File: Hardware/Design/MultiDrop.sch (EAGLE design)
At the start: 26 parts

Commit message: Hardware: ^9 rdy for review
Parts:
- removed SD1: SD, Documentation:SD
- added D3: DAYNIGHT, D-LED:LED5MM
- added D4: STATUS, D-LED:LED5MM
- added K1, K2, K3: (no value), L-PWR:L0805
- added U$12: FT, Documentation:FT
- D1: value (none) -> DAYNIGHT; device D-SBR:DSMC -> D-LED:LED5MM
- D2: value (none) -> STATUS; device D-SBR:DSMC -> D-LED:LED5MM
- R1, R2, R3, R4: value 50 -> 49.9
- U$11: value TT -> PT; device Documentation:TT -> Documentation:PT
- U$4: value FT -> K3; device Documentation:FT -> Documentation:K3
- U$6: value PT -> TT; device Documentation:PT -> Documentation:TT
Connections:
- removed net N$27: BM1.SPI, SD1.PV_PWR
- new net BL: K1.1, U$4.K1
- new net BL-WHT: K1.2, U$4.COM
- new net GN: K3.1, U$4.K3
- new net GN-WHT: K3.2
- new net N$40: BM1.0V@5, D2.K
- new net N$42: BM1.PWR, U$9.+BAT
- new net N$46: BM1.0V@6, D1.K
- new net N$47: BM1.17MA@0, U$5.PWR
- new net N$49: BM1.ICP1, U$5.PL
- new net N$50: BM1.20MA@0, U$6.PWR
- new net N$51: BM1.ADC0, R1.1, U$6.4TO20
- new net N$52: BM1.ADC1, R2.1, U$11.PWR
- new net N$53: BM1.20MA@1, U$11.4TO20
- new net N$54: BM3.20MA@2, BM3.ADC2, D4.A
- new net N$55: BM3.20MA@3, BM3.ADC3, D3.A
- new net N$56: BM3.0V@5, D4.K
- new net N$57: BM3.0V@6, D3.K
- new net OG: K2.1, U$4.K2
- new net OG-WHT: K2.2
- net N$12: now also BM1.0V@2, PV2.-PV, U$9.-BAT; no longer BM3.PWR, D2.K, U$7.BAT_PWR
- net N$13: now also BM3.0V@2, PV4.-PV, U$7.-BAT; no longer D2.A, PV4.PV_PWR
- net N$15: now also BM3.ALT, PV4.+PV; no longer BM1.PWR, D1.K, U$9.BAT_PWR
- net N$16: now also BM3.PWR, U$7.+BAT; no longer D1.A, PV2.PV_PWR
- net N$17: now also BM1.5V, U$4.SUPPLY, U$4.VCC; no longer BM1.0V@3, R1.2, R2.1
- net N$19: now also BM1.DIO13, U$4.E3; no longer BM1.20MA@0, U$11.PWR
- net N$20: now also BM1.0V@3, R1.2, R2.2, U$4.!E1, U$4.!E2, U$4.0V, U$4.0V@1; no longer BM1.ADC0, R1.1, U$11.4TO20
- net N$22: now also BM1.ALT, PV2.+PV; no longer BM1.0V@4, U$4.0V
- net N$23: now also BM3.17MA@0, U$12.PWR; no longer BM1.ICP1, U$4.OC
- net N$24: now also BM1.DIO10, U$4.A0; no longer BM1.17MA@0, U$4.PWR
- net N$25: now also BM1.DIO11, U$4.A1; no longer BM1.ADC1, R2.2, U$6.PWR
- net N$26: now also BM1.DIO12, U$4.A2; no longer BM1.20MA@1, U$6.4TO20
- net N$35: now also BM3.ICP1, U$12.PL; no longer BM3.0V@4, U$5.0V
- net N$36: now also BM1.20MA@2, BM1.ADC2, D2.A; no longer BM3.ICP1, U$5.OC
- net N$37: now also BM1.20MA@3, BM1.ADC3, D1.A; no longer BM3.17MA@0, U$5.PWR
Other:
- moved on the sheet: R1, R2

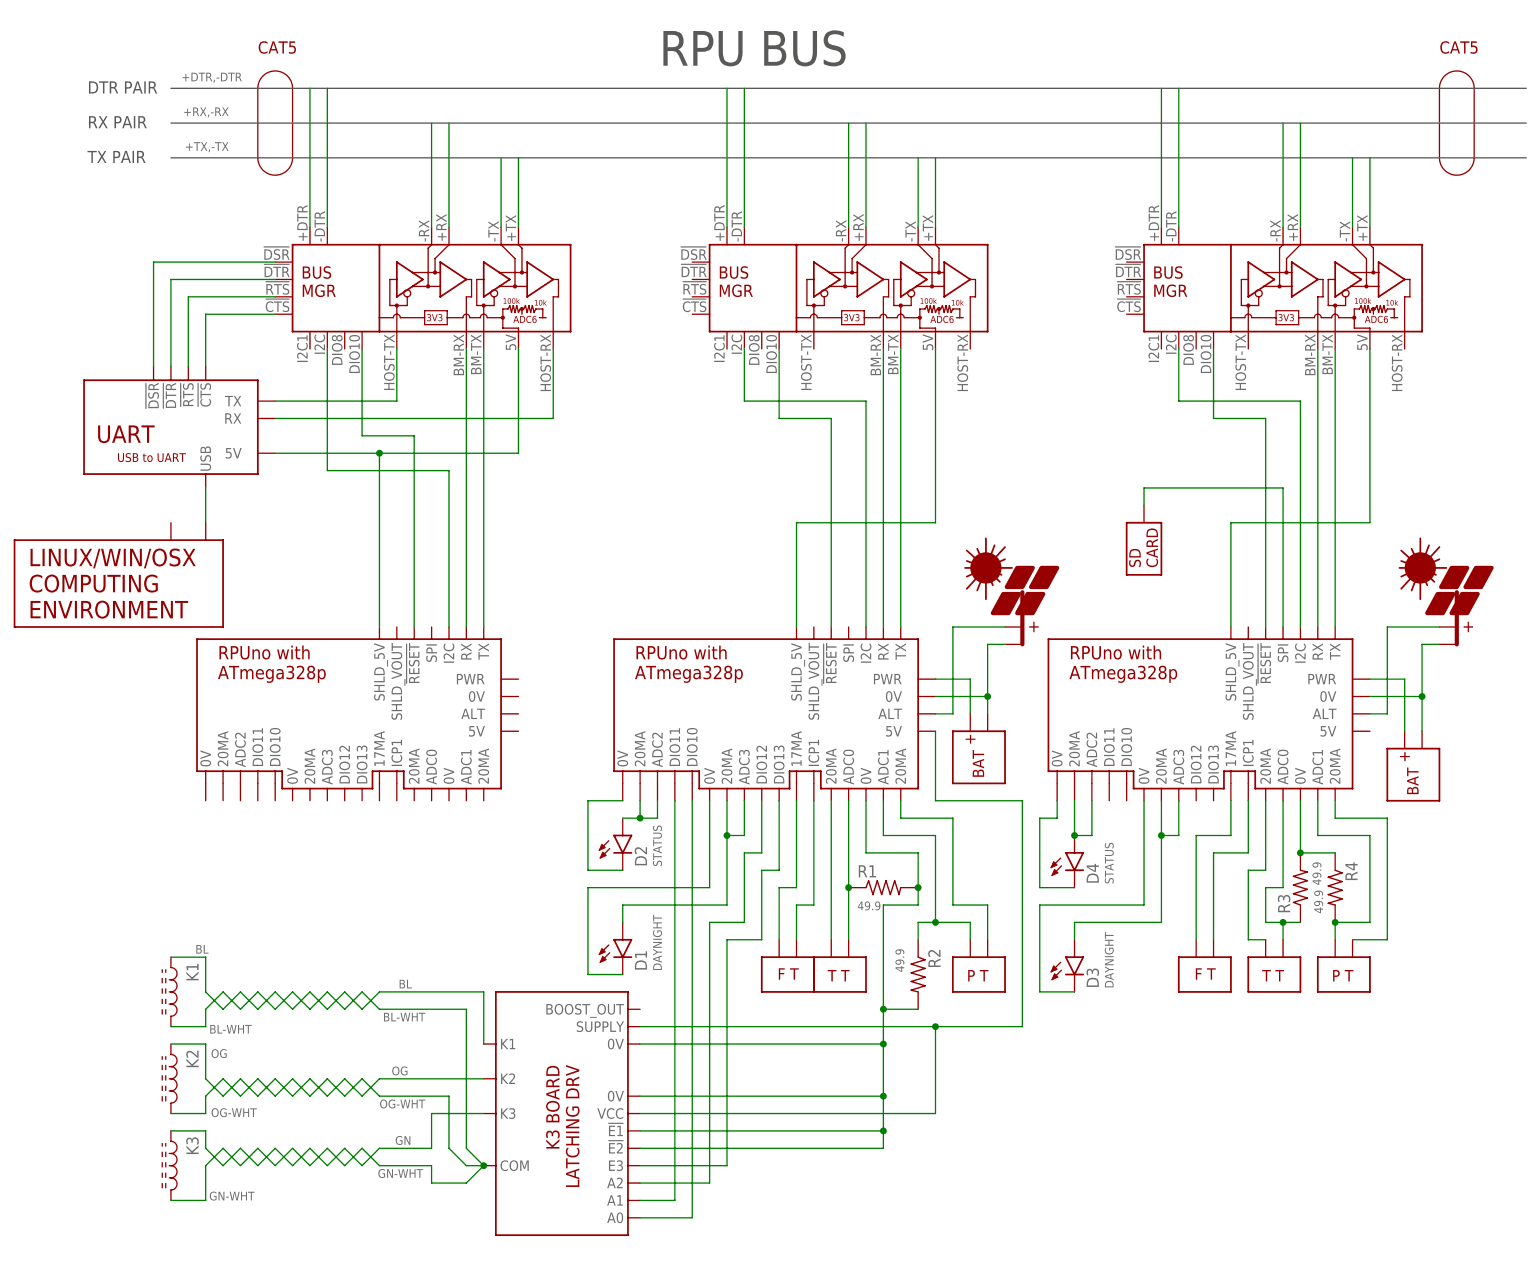
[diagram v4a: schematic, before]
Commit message: Hardware: PWR_I sense, SHLD_VIN gate stress
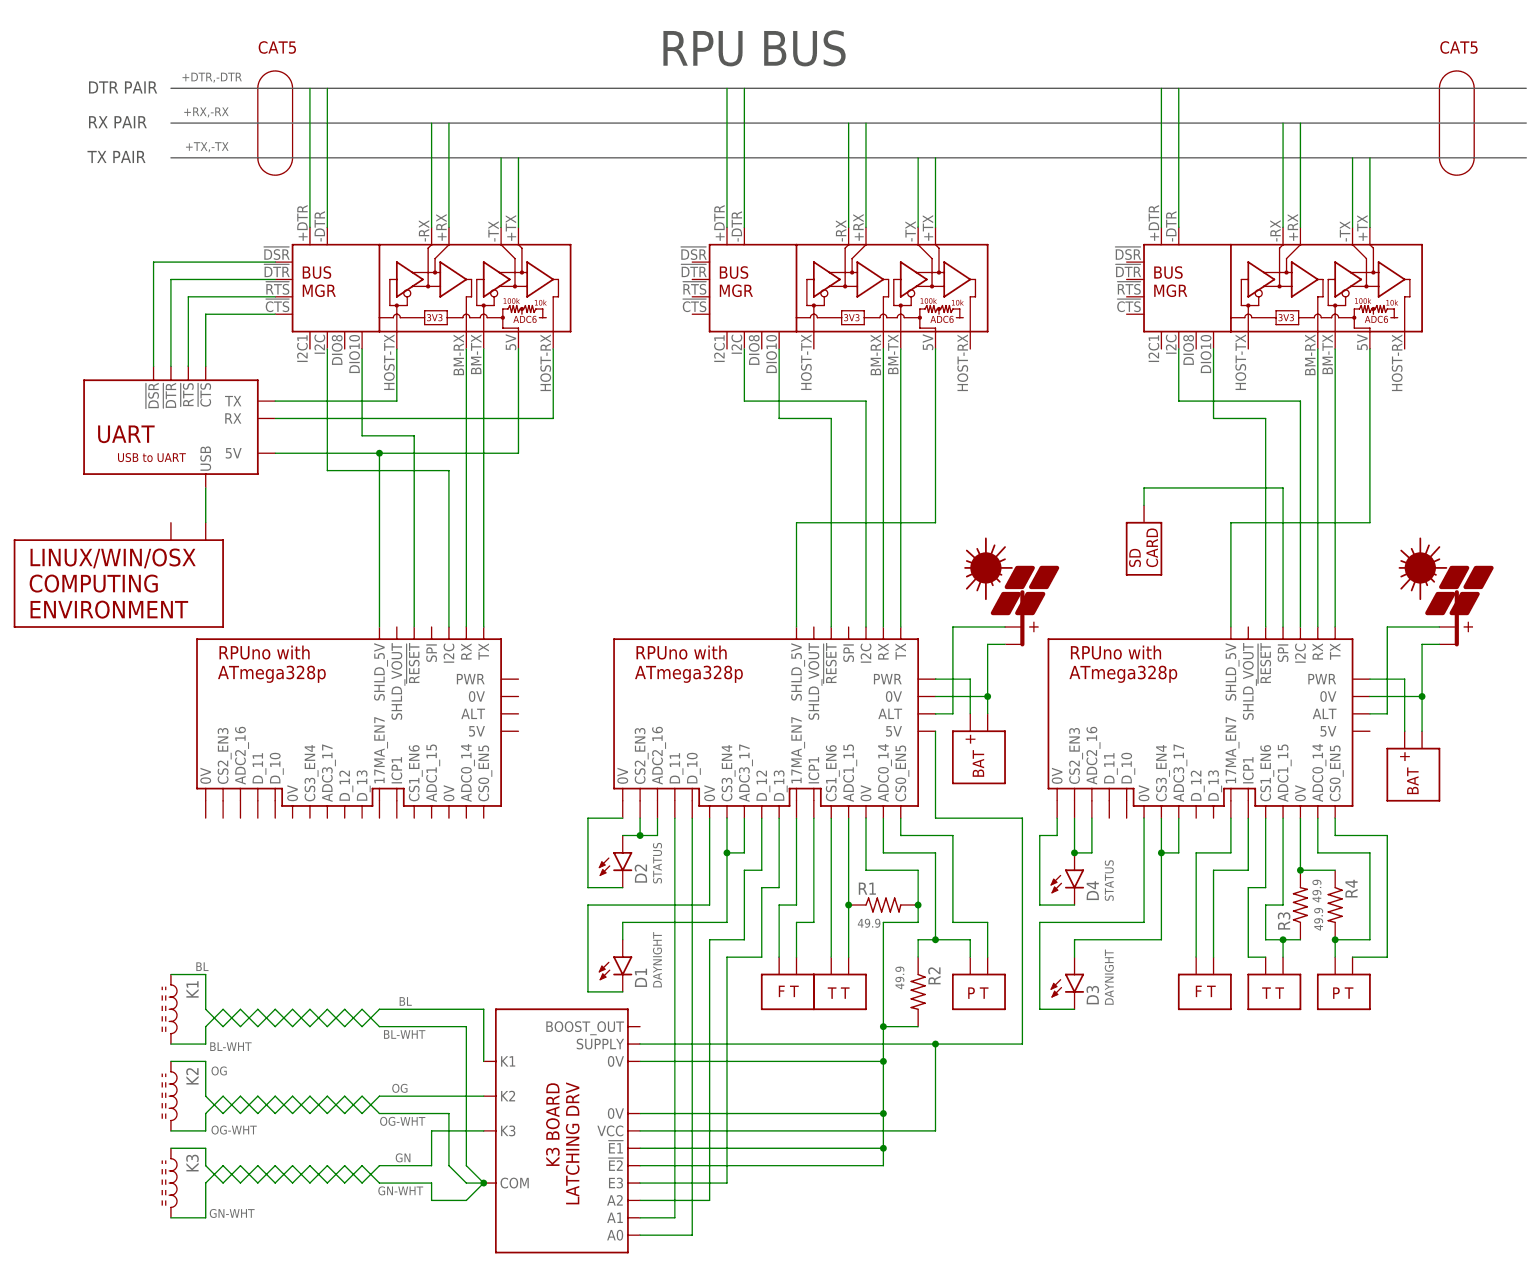
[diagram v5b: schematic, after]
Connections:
- net N$19: now also BM1.D_13; no longer BM1.DIO13
- net N$23: now also BM3.17MA_EN7; no longer BM3.17MA@0
- net N$24: now also BM1.D_10; no longer BM1.DIO10
- net N$25: now also BM1.D_11; no longer BM1.DIO11
- net N$26: now also BM1.D_12; no longer BM1.DIO12
- net N$31: now also BM3.ADC1_15; no longer BM3.ADC0
- net N$34: now also BM3.CS1_EN6; no longer BM3.20MA@0
- net N$36: now also BM1.ADC2_16, BM1.CS2_EN3; no longer BM1.20MA@2, BM1.ADC2
- net N$37: now also BM1.ADC3_17, BM1.CS3_EN4; no longer BM1.20MA@3, BM1.ADC3
- net N$38: now also BM3.ADC0_14; no longer BM3.ADC1
- net N$39: now also BM3.CS0_EN5; no longer BM3.20MA@1
- net N$47: now also BM1.17MA_EN7; no longer BM1.17MA@0
- net N$50: now also BM1.CS1_EN6; no longer BM1.20MA@0
- net N$51: now also BM1.ADC1_15; no longer BM1.ADC0
- net N$52: now also BM1.ADC0_14; no longer BM1.ADC1
- net N$53: now also BM1.CS0_EN5; no longer BM1.20MA@1
- net N$54: now also BM3.ADC2_16, BM3.CS2_EN3; no longer BM3.20MA@2, BM3.ADC2
- net N$55: now also BM3.ADC3_17, BM3.CS3_EN4; no longer BM3.20MA@3, BM3.ADC3
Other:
- moved on the sheet: D1, D2, D3, D4, K1, K2, K3, R1, R2, R3, R4

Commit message: Hardware: tested two boards to list on tindie
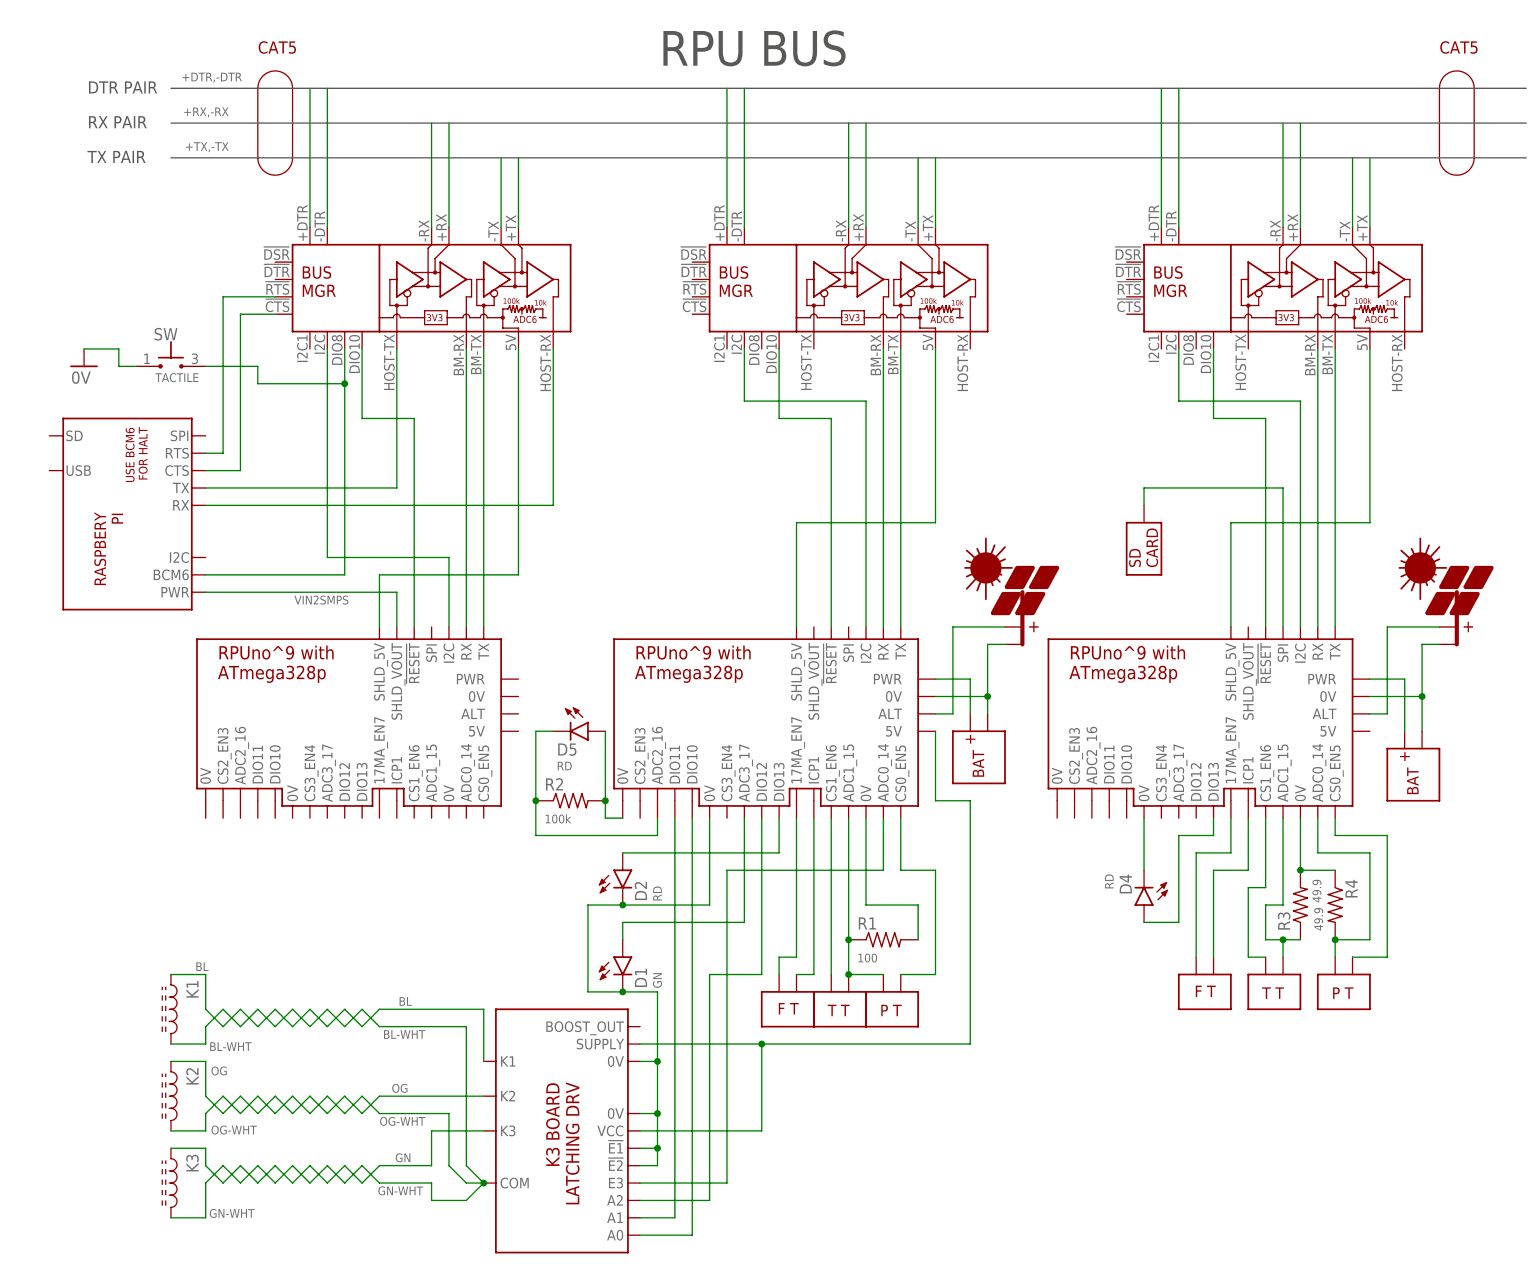
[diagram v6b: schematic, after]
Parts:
- removed D3: DAYNIGHT, D-LED:LED5MM
- removed PM1: (no value), Documentation:DESKTOP
- removed UART1: (no value), Documentation:UART
- added D5: RD, D-LED:LED5MM
- added SW: TACTILE, S-Tactile:TAC_SW
- added U$13: PI, Documentation:PI
- D1: value DAYNIGHT -> GN
- D2, D4: value STATUS -> RD
- R1: value 49.9 -> 100
- R2: value 49.9 -> 100k
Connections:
- removed net N$46: BM1.0V@6, D1.K
- removed net N$52: BM1.ADC0_14, R2.1, U$11.PWR
- removed net N$54: BM3.ADC2_16, BM3.CS2_EN3, D4.A
- removed net N$55: BM3.ADC3_17, BM3.CS3_EN4, D3.A
- removed net N$57: BM3.0V@6, D3.K
- new net 0V: SW.1
- new net N$27: BM1.0V@3, R1.2
- new net VIN2SMPS: BM2.SHLD_VOUT, U$13.PWR
- net N$19: now also BM1.ADC0_14; no longer BM1.D_13
- net N$20: now also BM3.DIO13, D4.A; no longer BM1.0V@3, R1.2, R2.2, U$4.!E1, U$4.!E2, U$4.0V, U$4.0V@1
- net N$24: now also BM1.DIO10; no longer BM1.D_10
- net N$25: now also BM1.DIO11; no longer BM1.D_11
- net N$26: now also BM1.DIO12; no longer BM1.D_12
- net N$29: no longer UART1.5V
- net N$3: now also SW.3, U$13.BCM6, U$3.DIO8; no longer PM1.TX, UART1.USB
- net N$36: now also BM1.DIO13; no longer BM1.ADC2_16, BM1.CS2_EN3
- net N$37: no longer BM1.CS3_EN4
- net N$4: now also U$13.CTS; no longer UART1.!CTS
- net N$40: now also BM1.0V@6, D1.K, U$4.!E1, U$4.!E2, U$4.0V, U$4.0V@1; no longer BM1.0V@5
- net N$5: now also U$13.RTS; no longer UART1.!RTS
- net N$51: now also U$11.PWR
- net N$56: now also BM3.0V@6; no longer BM3.0V@5
- net N$6: now also BM1.0V@5, D5.A, R2.2; no longer U$3.!DTR, UART1.!DTR
- net N$7: now also BM1.ADC2_16, D5.K, R2.1; no longer U$3.!DSR, UART1.!DSR
- net N$8: now also U$13.RX; no longer UART1.RX
- net N$9: now also U$13.TX; no longer UART1.TX
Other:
- note added: "DAY-NIGHT"
- note added: "LIGHT SENSOR"
- note added: "PI SHUTDOWN"
- note added: "READ PT CS1 OFF CS0 ON"
- note added: "READ TT CS1 ON CS0 OFF"
- note added: "RPUpi"
- note added: "STATUS"
- note removed: "RPUftdi"
- moved on the sheet: D2, D4, R1, R2
